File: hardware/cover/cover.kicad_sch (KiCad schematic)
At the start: 10 parts

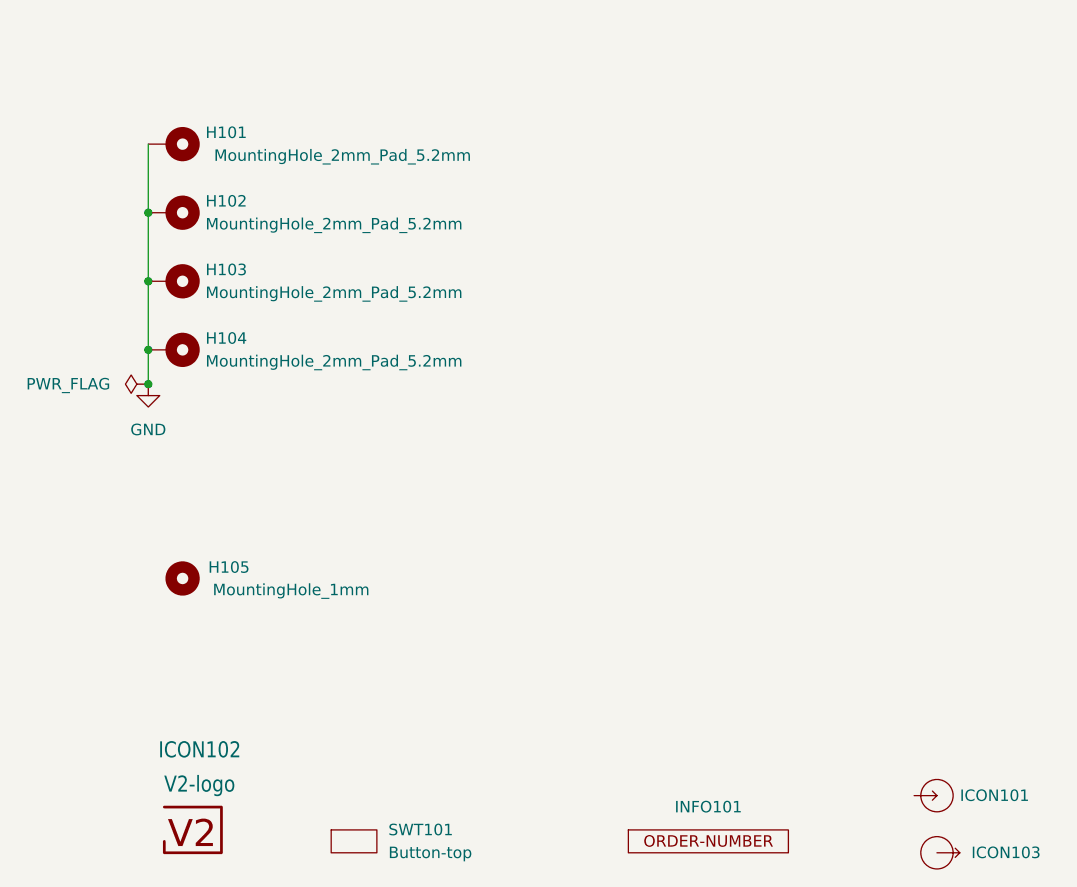
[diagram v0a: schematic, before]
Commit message: Replace Order_Number
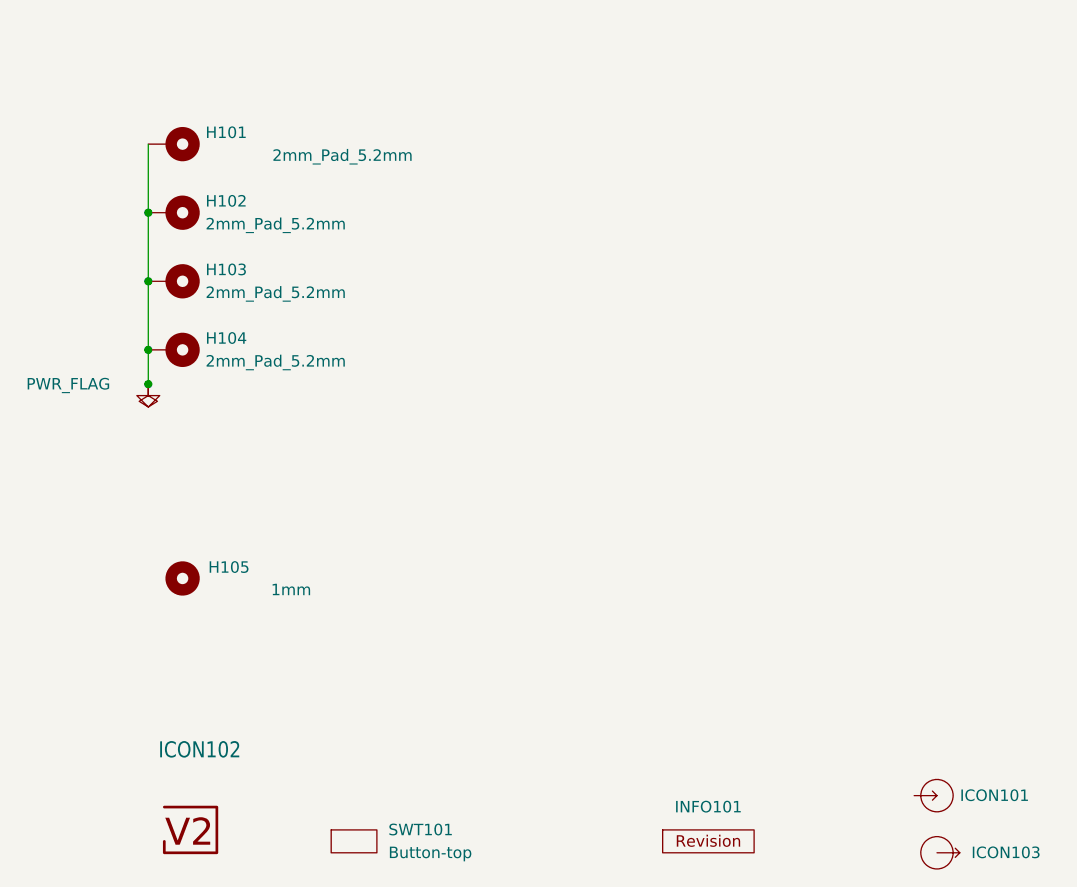
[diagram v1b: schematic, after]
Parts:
- H101, H102, H103, H104: value MountingHole_2mm_Pad_5.2mm -> 2mm_Pad_5.2mm
- H105: value MountingHole_1mm -> 1mm
- INFO101: value ORDER-NUMBER -> ~; footprint V2_Production:Order_Number -> V2_Production:Revision; symbol V2_Production:Order_Number -> V2_Production:Revision
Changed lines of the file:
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@@
 	(title_block
 		(title "V2 radio")
-		(date "2025-10-09")
-		(rev "1")
+		(date "2026-02-13")
+		(rev "2025-10-09")
 		(company "Versio Duo")
 		(comment 1 "Cover")
@@
 	)
 	(symbol
-		(lib_id "power:GND")
+		(lib_id "V2_power:GND")
 		(at 138.43 85.09 0)
 		(unit 1)
@@
 					(size 1.27 1.27)
 				)
+				(hide yes)
 			)
 		)
@@
 		(at 140.97 66.04 270)
 		(unit 1)
-		(exclude_from_sim yes)
+		(exclude_from_sim no)
 		(in_bom no)
 		(on_board yes)
@@
 			)
 		)
-		(property "Value" "MountingHole_2mm_Pad_5.2mm"
+		(property "Value" "2mm_Pad_5.2mm"
 			(at 144.78 67.3099 90)
 			(effects
@@
 			)
 		)
-		(property "Description" ""
+		(property "Description" "Mounting Hole with connection"
 			(at 140.97 66.04 0)
 			(effects
@@
 	)
 	(symbol
-		(lib_id "V2_Production:Order_Number")
+		(lib_id "V2_Production:Revision")
 		(at 200.66 135.89 0)
 		(unit 1)
-		(exclude_from_sim yes)
+		(exclude_from_sim no)
 		(in_bom no)
 		(on_board yes)
@@
 			)
 		)
-		(property "Value" "ORDER-NUMBER"
+		(property "Value" "~"
 			(at 200.66 138.43 0)
 			(effects
@@
 			)
 		)
-		(property "Footprint" "V2_Production:Order_Number"
+		(property "Footprint" "V2_Production:Revision"
 			(at 200.66 140.97 0)
 			(effects
@@
 		(at 161.29 135.89 0)
 		(unit 1)
-		(exclude_from_sim yes)
+		(exclude_from_sim no)
 		(in_bom no)
 		(on_board yes)
@@
 			)
 		)
+		(property "Sim.Enable" "0"
+			(at 161.29 135.89 0)
+			(effects
+				(font
+					(size 1.27 1.27)
+				)
+				(hide yes)
+			)
+		)
 		(instances
 			(project "control-cover"
@@
 		(at 140.97 81.28 270)
 		(unit 1)
-		(exclude_from_sim yes)
+		(exclude_from_sim no)
 		(in_bom no)
 		(on_board yes)
@@
 			)
 		)
-		(property "Value" "MountingHole_2mm_Pad_5.2mm"
+		(property "Value" "2mm_Pad_5.2mm"
 			(at 144.78 82.5499 90)
 			(effects
@@
 			)
 		)
-		(property "Description" ""
+		(property "Description" "Mounting Hole with connection"
 			(at 140.97 81.28 0)
 			(effects
@@
 		(at 140.97 58.42 270)
 		(unit 1)
-		(exclude_from_sim yes)
+		(exclude_from_sim no)
 		(in_bom no)
 		(on_board yes)
@@
 			)
 		)
-		(property "Value" "MountingHole_2mm_Pad_5.2mm"
+		(property "Value" "2mm_Pad_5.2mm"
 			(at 160.02 59.6899 90)
 			(effects
@@
 			)
 		)
-		(property "Description" ""
+		(property "Description" "Mounting Hole with connection"
 			(at 140.97 58.42 0)
 			(effects
@@
 	)
 	(symbol
-		(lib_id "power:PWR_FLAG")
+		(lib_id "V2_power:PWR_FLAG")
 		(at 138.43 85.09 90)
 		(unit 1)
@@
 			)
 		)
-		(property "Datasheet" "~"
+		(property "Datasheet" ""
 			(at 138.43 85.09 0)
 			(effects
@@
 			)
 		)
-		(property "Description" ""
+		(property "Description" "Special symbol for telling ERC where power comes from"
 			(at 138.43 85.09 0)
 			(effects
@@
 		(at 142.24 106.68 0)
 		(unit 1)
-		(exclude_from_sim yes)
+		(exclude_from_sim no)
 		(in_bom no)
 		(on_board yes)
@@
 			)
 		)
-		(property "Value" "MountingHole_1mm"
+		(property "Value" "1mm"
 			(at 154.305 107.95 0)
 			(effects
@@
 			)
 		)
-		(property "Description" ""
+		(property "Description" "Mounting Hole without connection"
 			(at 142.24 106.68 0)
 			(effects
@@
 		(at 143.51 134.62 0)
 		(unit 1)
-		(exclude_from_sim yes)
+		(exclude_from_sim no)
 		(in_bom no)
 		(on_board yes)
@@
 					(size 1.778 1.5113)
 				)
+				(hide yes)
 			)
 		)
@@
 		(at 140.97 73.66 270)
 		(unit 1)
-		(exclude_from_sim yes)
+		(exclude_from_sim no)
 		(in_bom no)
 		(on_board yes)
@@
 			)
 		)
-		(property "Value" "MountingHole_2mm_Pad_5.2mm"
+		(property "Value" "2mm_Pad_5.2mm"
 			(at 144.78 74.9299 90)
 			(effects
@@
 			)
 		)
-		(property "Description" ""
+		(property "Description" "Mounting Hole with connection"
 			(at 140.97 73.66 0)
 			(effects

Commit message: Update Library
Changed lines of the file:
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@@
-	)
-	(junction
-		(at 138.43 85.09)
-		(diameter 0)
-		(color 0 0 0 0)
 	)
 	(junction
@@
 		(dnp no)
 		(fields_autoplaced yes)
-		(property "Reference" "#PWR0101"
+		(property "Reference" "#PWR101"
 			(at 138.43 91.44 0)
 			(effects
@@
 			(project "control-cover"
 				(path "/6c8448b4-b04d-47e1-934e-e40cbe27a7be"
-					(reference "#PWR0101")
+					(reference "#PWR101")
 					(unit 1)
 				)
@@
 		(at 226.06 130.81 0)
 		(unit 1)
-		(exclude_from_sim no)
+		(exclude_from_sim yes)
 		(in_bom no)
 		(on_board yes)
@@
 			)
 		)
-		(property "Sim.Enable" "0"
-			(at 226.06 130.81 0)
-			(effects
-				(font
-					(size 1.27 1.27)
-				)
-				(hide yes)
-			)
-		)
 		(instances
 			(project ""
 				(path "/6c8448b4-b04d-47e1-934e-e40cbe27a7be"
 					(reference "ICON101")
+					(unit 1)
+				)
+			)
+		)
+	)
+	(symbol
+		(lib_id "V2_power:GND")
+		(at 149.86 45.72 90)
+		(unit 1)
+		(exclude_from_sim no)
+		(in_bom yes)
+		(on_board yes)
+		(dnp no)
+		(fields_autoplaced yes)
+		(property "Reference" "#PWR0102"
+			(at 156.21 45.72 0)
+			(effects
+				(font
+					(size 1.27 1.27)
+				)
+				(hide yes)
+			)
+		)
+		(property "Value" "GND"
+			(at 154.94 45.72 0)
+			(effects
+				(font
+					(size 1.27 1.27)
+				)
+				(hide yes)
+			)
+		)
+		(property "Footprint" ""
+			(at 149.86 45.72 0)
+			(effects
+				(font
+					(size 1.27 1.27)
+				)
+				(hide yes)
+			)
+		)
+		(property "Datasheet" ""
+			(at 149.86 45.72 0)
+			(effects
+				(font
+					(size 1.27 1.27)
+				)
+				(hide yes)
+			)
+		)
+		(property "Description" ""
+			(at 149.86 45.72 0)
+			(effects
+				(font
+					(size 1.27 1.27)
+				)
+				(hide yes)
+			)
+		)
+		(pin "1"
+		)
+		(instances
+			(project "cover"
+				(path "/6c8448b4-b04d-47e1-934e-e40cbe27a7be"
+					(reference "#PWR0102")
 					(unit 1)
 				)
@@
 		(at 161.29 135.89 0)
 		(unit 1)
-		(exclude_from_sim no)
+		(exclude_from_sim yes)
 		(in_bom no)
 		(on_board yes)
@@
 			)
 		)
-		(property "Sim.Enable" "0"
-			(at 161.29 135.89 0)
-			(effects
-				(font
-					(size 1.27 1.27)
-				)
-				(hide yes)
-			)
-		)
 		(instances
 			(project "control-cover"
@@
 		)
 		(property "Value" "2mm_Pad_5.2mm"
-			(at 160.02 59.6899 90)
+			(at 153.162 59.6899 90)
 			(effects
 				(font
@@
 		(at 226.06 137.16 0)
 		(unit 1)
-		(exclude_from_sim no)
+		(exclude_from_sim yes)
 		(in_bom no)
 		(on_board yes)
@@
 			)
 		)
-		(property "Sim.Enable" "0"
-			(at 226.06 137.16 0)
-			(effects
-				(font
-					(size 1.27 1.27)
-				)
-				(hide yes)
-			)
-		)
 		(instances
 			(project ""
@@
 	(symbol
 		(lib_id "V2_power:PWR_FLAG")
-		(at 138.43 85.09 90)
+		(at 149.86 45.72 0)
 		(unit 1)
 		(exclude_from_sim no)
@@
 		(on_board yes)
 		(dnp no)
-		(property "Reference" "#FLG0101"
-			(at 136.525 85.09 0)
+		(property "Reference" "#FLG101"
+			(at 149.86 43.815 0)
 			(effects
 				(font
@@
 		)
 		(property "Value" "PWR_FLAG"
-			(at 129.54 85.09 90)
+			(at 138.176 45.72 0)
 			(effects
 				(font
@@
 		)
 		(property "Footprint" ""
-			(at 138.43 85.09 0)
-			(effects
-				(font
-					(size 1.27 1.27)
-				)
-				(hide yes)
-			)
-		)
-		(property "Datasheet" ""
-			(at 138.43 85.09 0)
+			(at 149.86 45.72 0)
+			(effects
+				(font
+					(size 1.27 1.27)
+				)
+				(hide yes)
+			)
+		)
+		(property "Datasheet" ""
+			(at 149.86 45.72 0)
 			(effects
 				(font
@@
 		)
 		(property "Description" "Special symbol for telling ERC where power comes from"
-			(at 138.43 85.09 0)
+			(at 149.86 45.72 0)
 			(effects
 				(font
@@
 		)
 		(instances
-			(project "control-cover"
-				(path "/6c8448b4-b04d-47e1-934e-e40cbe27a7be"
-					(reference "#FLG0101")
+			(project "cover"
+				(path "/6c8448b4-b04d-47e1-934e-e40cbe27a7be"
+					(reference "#FLG101")
 					(unit 1)
 				)
@@
 		)
 		(property "Value" "1mm"
-			(at 154.305 107.95 0)
-			(effects
-				(font
+			(at 147.447 107.95 0)
+			(effects
+				(font
